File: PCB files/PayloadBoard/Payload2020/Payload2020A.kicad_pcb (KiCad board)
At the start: 2 copper layers, 38.1 x 127 mm, 24 parts, among them J1 BATTERY, J2 BridgeConn, J3 LoadCell, Q1 Q_NMOS_GSD, Q2 Q_NMOS_GSD, SW1 SW_SPST, U1 Teensy3.6, U2 ArduCam, U3 HX711_Breakout, U4 AP7370-50W5-7, U5 TPS613222ADBVR

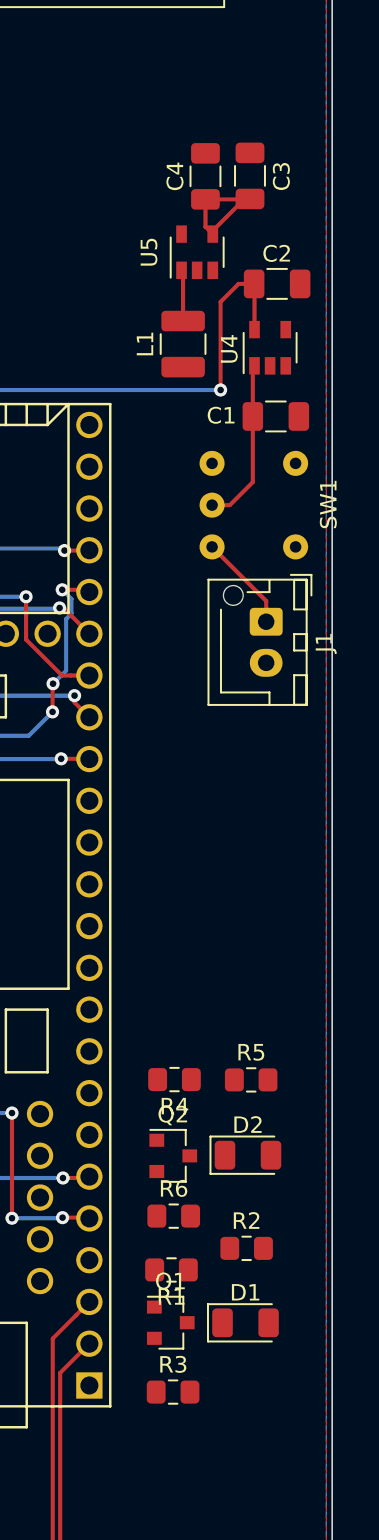
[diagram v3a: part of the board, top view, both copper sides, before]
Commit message: Minor visual changes to boards
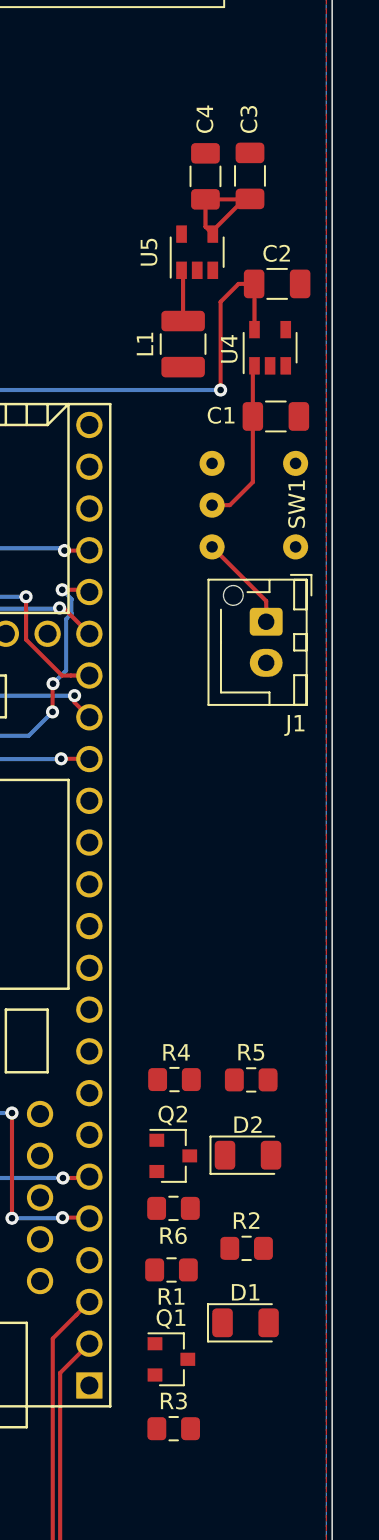
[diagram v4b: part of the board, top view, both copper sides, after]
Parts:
- moved Q1 2.23 mm to (150.6, 140.2)
- moved R3 2.23 mm to (150.7, 144.4)
- moved R6 0.47 mm to (150.7, 131.0)
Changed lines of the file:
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@@
     (tags capacitor)
     (attr smd)
-    (fp_text reference C3 (at -0.02032 1.9431 90) (layer F.SilkS)
+    (fp_text reference C3 (at 3.44932 -0.03048 90) (layer F.SilkS)
       (effects (font (size 1 1) (thickness 0.15)))
     )
@@
     (tags capacitor)
     (attr smd)
-    (fp_text reference C4 (at 0 -1.82 90) (layer F.SilkS)
+    (fp_text reference C4 (at 3.47726 -0.00254 90) (layer F.SilkS)
       (effects (font (size 1 1) (thickness 0.15)))
     )
@@
     (descr "JST XH series connector, B2B-XH-AM, with boss (http://www.jst-mfg.com/product/pdf/eng/eXH.pdf), generated with kicad-footprint-generator")
     (tags "connector JST XH vertical boss")
-    (fp_text reference J1 (at 1.25 -3.55 90) (layer F.SilkS)
+    (fp_text reference J1 (at 6.20776 -1.81356 180) (layer F.SilkS)
       (effects (font (size 1 1) (thickness 0.15)))
     )
@@
   )
   (module Package_TO_SOT_SMD:SOT-23 (layer F.Cu)
-    (at 150.56104 137.94994)
+    (at 150.5966 140.17752)
     (descr "SOT-23, Standard")
     (tags SOT-23)
@@
   )
   (module Resistor_SMD:R_0805_2012Metric_Pad1.15x1.40mm_HandSolder (layer F.Cu)
-    (at 150.70074 142.16888)
+    (at 150.7363 144.39646)
     (descr "Resistor SMD 0805 (2012 Metric), square (rectangular) end terminal, IPC_7351 nominal with elongated pad for handsoldering. (Body size source: https://docs.google.com/spreadsheets/d/1BsfQQcO9C6DZCsRaXUlFlo91Tg2WpOkGARC1WS5S8t0/edit?usp=sharing), generated with kicad-footprint-generator")
     (tags "resistor handsolder")
@@
     (tags "resistor handsolder")
     (attr smd)
-    (fp_text reference R4 (at 0 -1.65) (layer F.SilkS)
+    (fp_text reference R4 (at -0.09906 1.61798) (layer F.SilkS)
       (effects (font (size 1 1) (thickness 0.15)))
     )
@@
   )
   (module Resistor_SMD:R_0805_2012Metric_Pad1.15x1.40mm_HandSolder (layer F.Cu)
-    (at 150.7363 131.46786)
+    (at 150.7236 130.99796)
     (descr "Resistor SMD 0805 (2012 Metric), square (rectangular) end terminal, IPC_7351 nominal with elongated pad for handsoldering. (Body size source: https://docs.google.com/spreadsheets/d/1BsfQQcO9C6DZCsRaXUlFlo91Tg2WpOkGARC1WS5S8t0/edit?usp=sharing), generated with kicad-footprint-generator")
     (tags "resistor handsolder")
     (attr smd)
-    (fp_text reference R6 (at 0 -1.65) (layer F.SilkS)
+    (fp_text reference R6 (at -0.01778 1.6891) (layer F.SilkS)
       (effects (font (size 1 1) (thickness 0.15)))
     )
@@
   (module Payload:GW12RCH (layer F.Cu)
     (at 155.97632 88.21928 90)
-    (fp_text reference SW1 (at 0.0508 4.20116 90) (layer F.SilkS)
+    (fp_text reference SW1 (at 0.07112 2.2733 90) (layer F.SilkS)
       (effects (font (size 1 1) (thickness 0.15)))
     )
@@
   (gr_line (start 160.3755 51.77912) (end 160.3755 178.77912) (layer Edge.Cuts) (width 0.1))
   (gr_line (start 122.2755 178.77912) (end 160.3755 178.77912) (layer Edge.Cuts) (width 0.1))
-  (via (at 142.53718 153.46172) (size 0.8) (drill 0.4) (layers F.Cu B.Cu) (net 6))
   (segment (start 139.728041 96.847559) (end 140.52804 96.04756) (width 0.25) (layer F.Cu) (net 1))
   (segment (start 138.88466 97.69094) (end 139.728041 96.847559) (width 0.25) (layer F.Cu) (net 1))
   (segment (start 138.88466 154.45232) (end 138.88466 97.69094) (width 0.25) (layer F.Cu) (net 1))
   (segment (start 153.31186 168.87952) (end 138.88466 154.45232) (width 0.25) (layer F.Cu) (net 1))
+  (via (at 142.53718 153.46172) (size 0.8) (drill 0.4) (layers F.Cu B.Cu) (net 6))
   (segment (start 155.54914 86.82341) (end 155.54914 82.8294) (width 0.25) (layer F.Cu) (net 36))
   (segment (start 153.07056 88.22436) (end 154.14819 88.22436) (width 0.25) (layer F.Cu) (net 36))
@@
     (connect_pads (clearance 0.508))
     (min_thickness 0.254)
-    (fill (arc_segments 32) (thermal_gap 0.508) (thermal_bridge_width 0.508))
+    (fill yes (arc_segments 32) (thermal_gap 0.508) (thermal_bridge_width 0.508))
     (polygon
       (pts
@@
     (connect_pads (clearance 0.508))
     (min_thickness 0.254)
-    (fill (arc_segments 32) (thermal_gap 0.508) (thermal_bridge_width 0.508))
+    (fill yes (arc_segments 32) (thermal_gap 0.508) (thermal_bridge_width 0.508))
     (polygon
       (pts

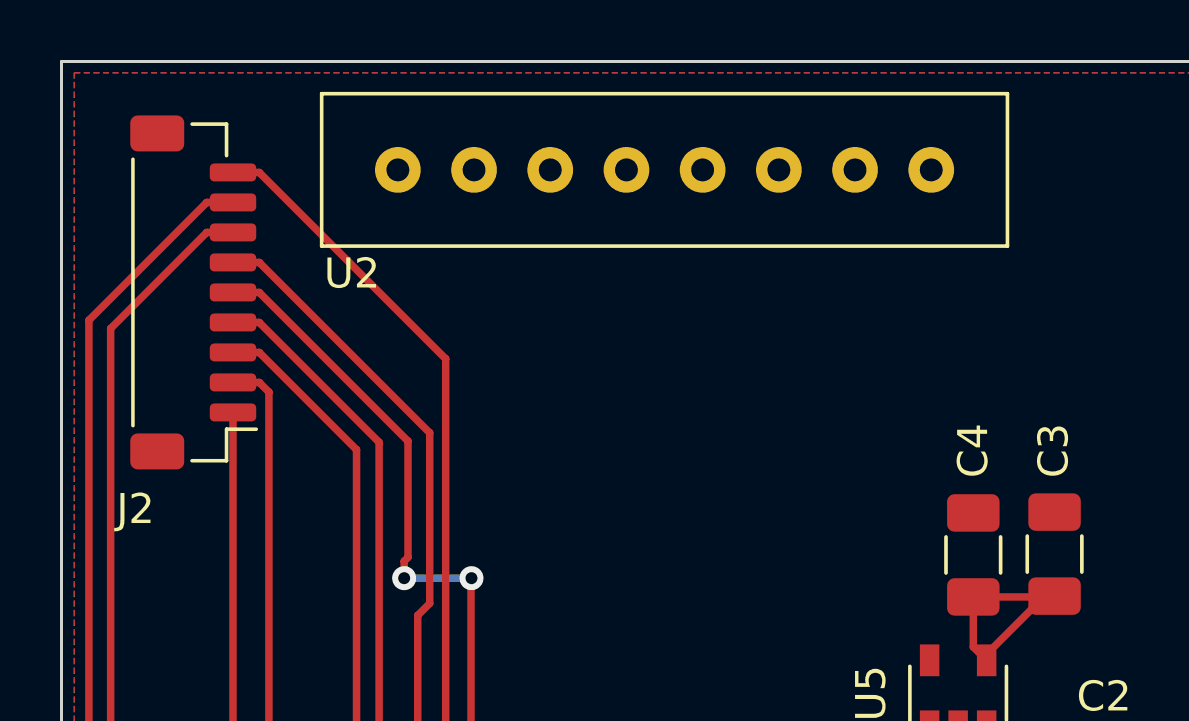
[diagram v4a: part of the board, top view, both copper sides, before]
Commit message: Began routing Board B Adjusted board bridge to 10 pins to transfer both 3.3v rails
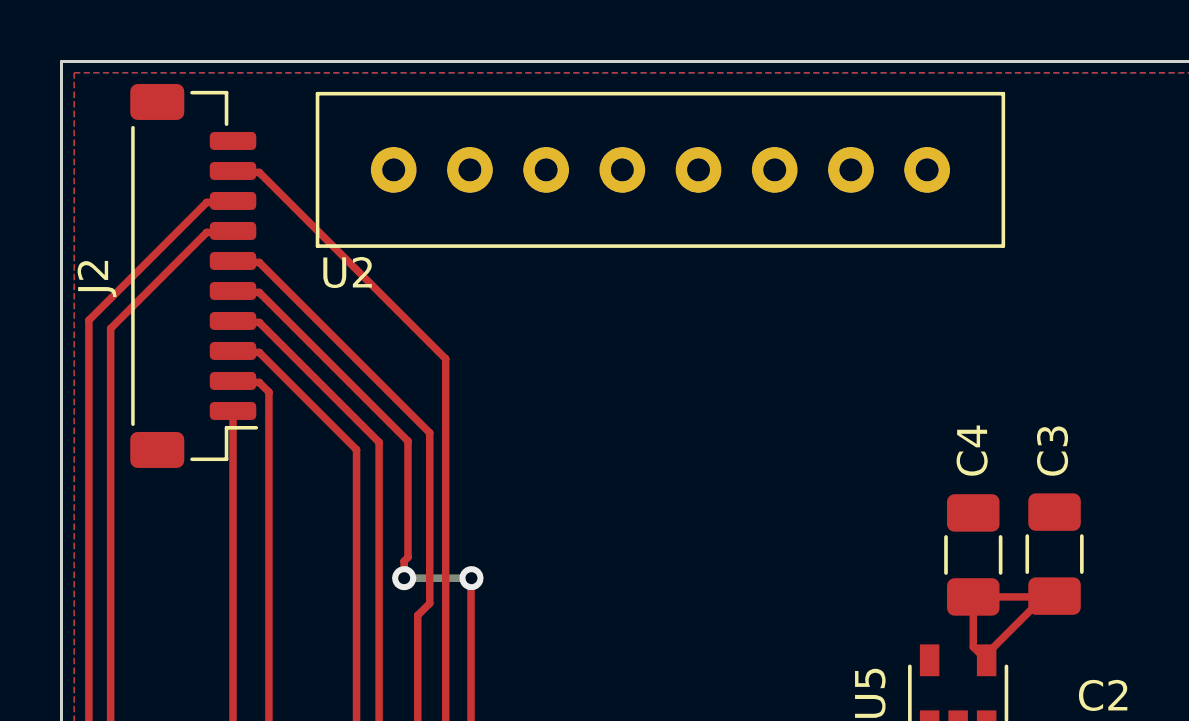
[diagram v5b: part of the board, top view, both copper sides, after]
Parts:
- J2: footprint Connector_JST:JST_SH_BM09B-SRSS-TB_1x09-1MP_P1.00mm_Vertical -> Connector_JST:JST_SH_BM10B-SRSS-TB_1x10-1MP_P1.00mm_Vertical
- moved J2 0.55 mm to (126.7, 58.9)
- moved U2 0.14 mm to (142.2, 55.1)

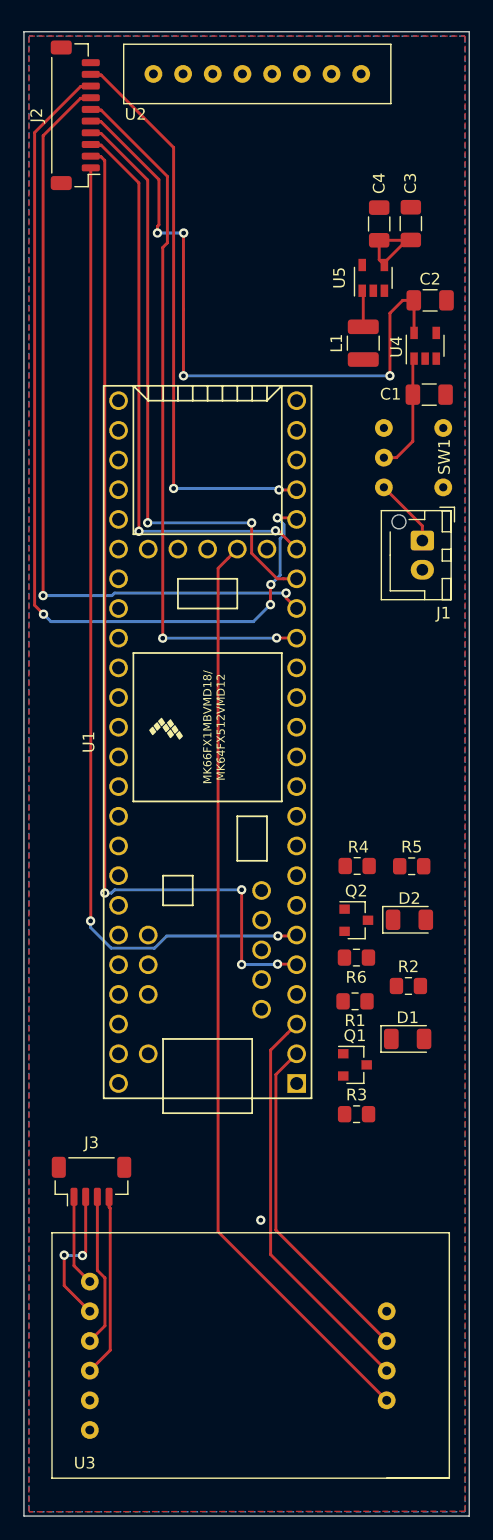
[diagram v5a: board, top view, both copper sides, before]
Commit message: Placed corner mounting holes on each board Drew backside ground plane on Board B
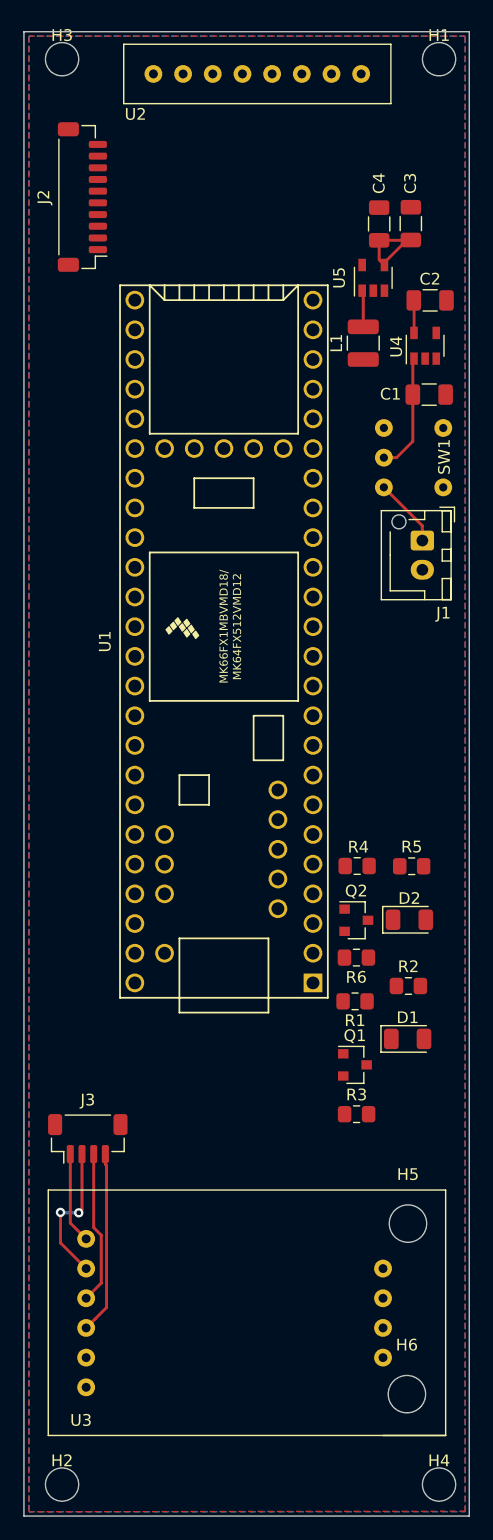
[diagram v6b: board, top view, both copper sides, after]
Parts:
- added H1: Corner, Payload:MountingHole_4-40, F.Cu at (157.8, 54.1)
- added H2: Corner, Payload:MountingHole_4-40, F.Cu at (125.5, 176.1)
- added H3: Corner, Payload:MountingHole_4-40, F.Cu at (125.5, 54.1)
- added H4: Corner, Payload:MountingHole_4-40, F.Cu at (157.8, 176.1)
- added H5: HX711, MountingHole:MountingHole_3.2mm_M3, F.Cu at (155.1, 153.8)
- added H6: HX711, MountingHole:MountingHole_3.2mm_M3, F.Cu at (155.0, 168.4)
- moved U1 8.72 mm to (139.4, 104.0)
- moved J2 7.02 mm to (127.3, 65.9)
- moved U3 3.67 mm to (139.7, 161.4)
- moved J3 3.67 mm to (127.7, 146.5)
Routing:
- net /Berry_SCL: track 87.0 -> 0.00 mm, vias 4 -> 0
- net /Berry_SDA: track 83.8 -> 0.00 mm, vias 2 -> 0
- net +3V3: track 79.5 -> 0.00 mm
- net /XBEE_DOUT: track 78.1 -> 0.00 mm, vias 4 -> 0
- net /XBEE_CTS: track 67.3 -> 0.00 mm, vias 2 -> 0
- net /XBEE_RTS: track 60.1 -> 0.00 mm, vias 2 -> 0
- net +3.3VA: track 55.3 -> 2.79 mm, vias 4 -> 0
- net /TX_GPS: track 52.1 -> 0.00 mm, vias 2 -> 0
- net /RX_GPS: track 49.4 -> 0.00 mm, vias 2 -> 0
- net /XBEE_DIN: track 49.4 -> 0.00 mm, vias 2 -> 0
- net /HX_CLK: track 34.7 -> 0.00 mm
- net /HX_OUT: track 29.2 -> 0.00 mm
- net GNDREF: vias 1 -> 0

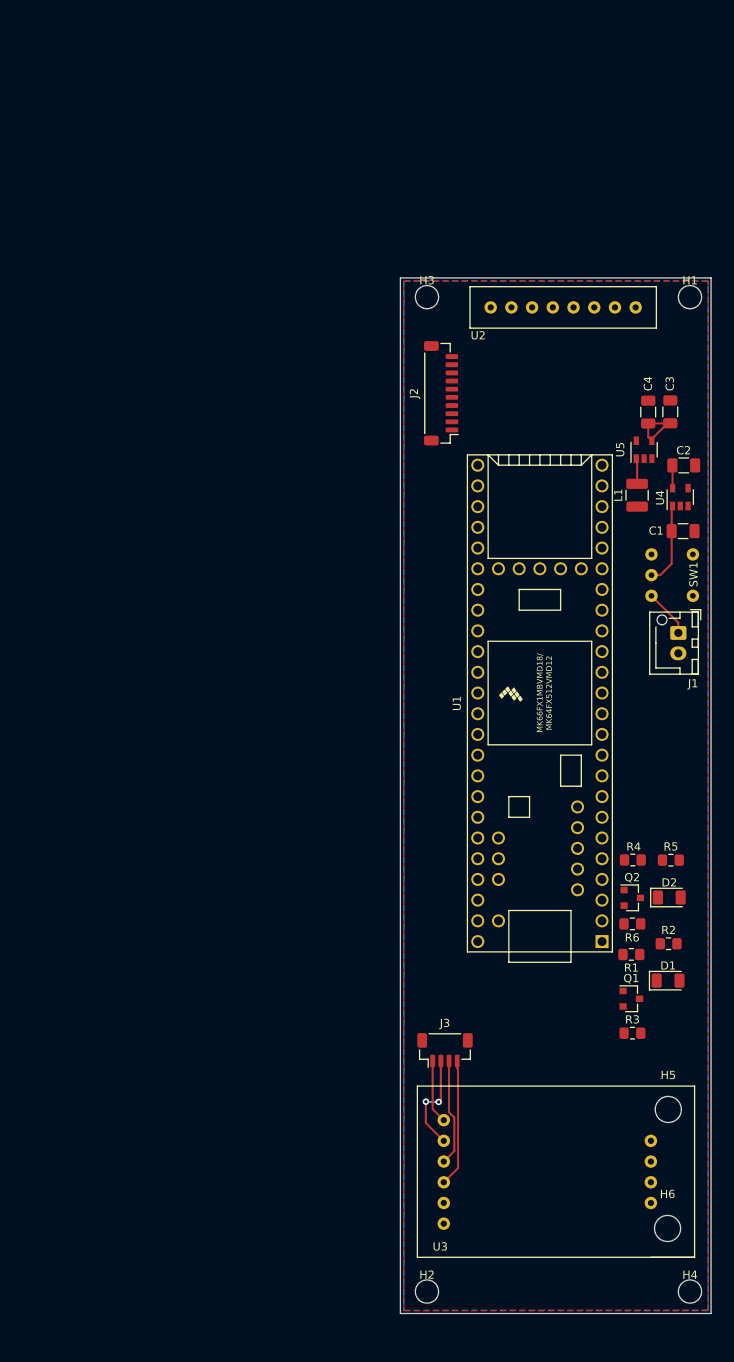
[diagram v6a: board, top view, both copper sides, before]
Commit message: Checked and fixed alignment of HX711 footprint dimensions Added hx711 mounting hole directly to footprint Redrawn edge cuts to fit into payload bay with about 0.01" fudge factor
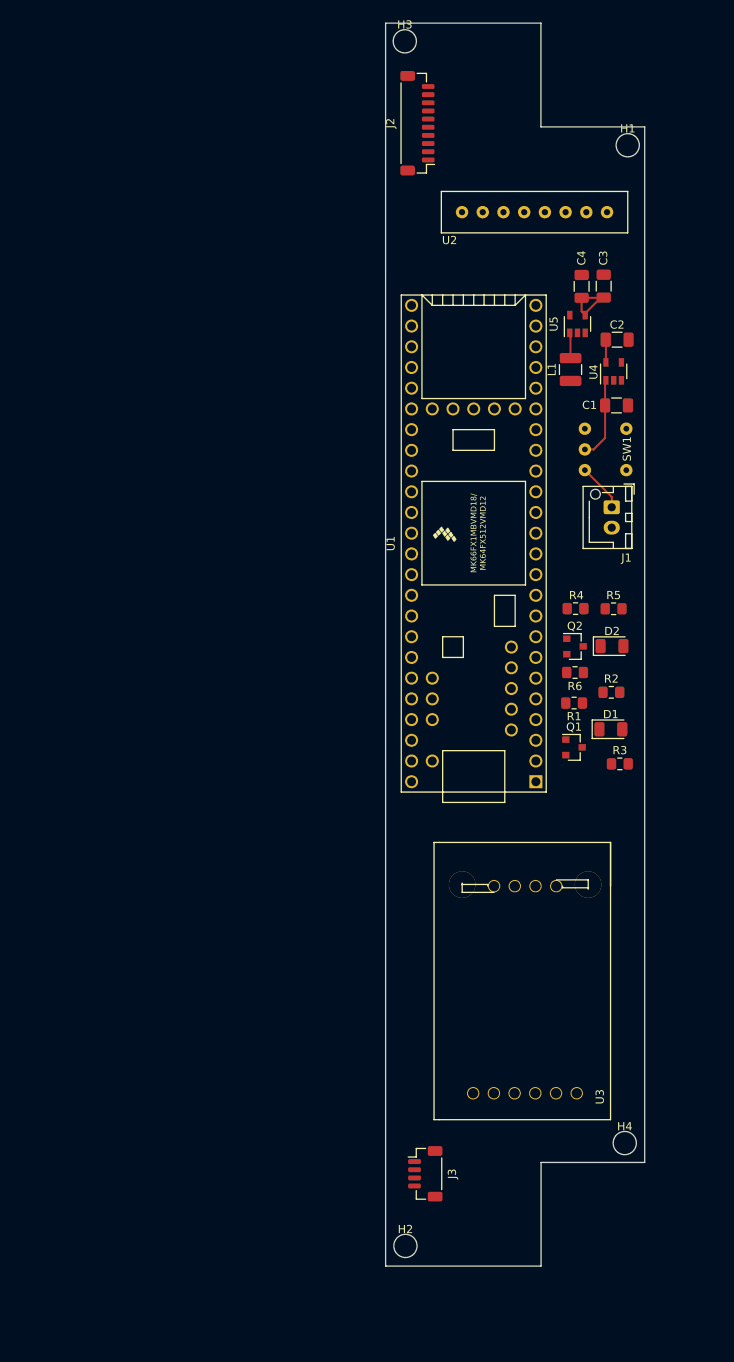
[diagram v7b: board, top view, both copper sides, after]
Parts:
- removed H5, H6: HX711, MountingHole:MountingHole_3.2mm_M3
- moved J2 33.3 mm to (124.4, 32.8)
- moved R3 33.1 mm to (149.2, 111.4)
- moved D1 31.6 mm to (148.1, 107.1)
- moved R2 31.6 mm to (148.1, 102.6)
- moved R6 31.6 mm to (143.7, 100.2)
- moved D2 31.6 mm to (148.2, 96.9)
- moved Q2 31.6 mm to (143.7, 97.0)
- moved R1 31.6 mm to (143.6, 103.9)
- moved R4 31.6 mm to (143.8, 92.3)
- moved Q1 31.6 mm to (143.6, 109.3)
- moved R5 31.6 mm to (148.4, 92.4)
- moved H3 31.5 mm to (122.8, 22.8)
- moved U3 21.8 mm to (137.6, 139.7), turned to 90 degrees
- moved U1 21.2 mm to (131.3, 84.4)
- moved H1 20.1 mm to (150.2, 35.5)
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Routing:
- net Net-(J3-Pad4): track 15.6 -> 0.00 mm
- net Net-(J3-Pad3): track 13.1 -> 0.00 mm
- net Net-(J3-Pad2): track 12.4 -> 0.00 mm, vias 2 -> 0
- net Net-(J3-Pad1): track 7.82 -> 0.00 mm
- removed copper zone on B.Cu, net GNDREF
- removed copper zone on F.Cu, net GNDREF
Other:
- board size 38.1 x 127 mm -> 31.8 x 152.4 mm
- board text removed: "TOP of BAY"
